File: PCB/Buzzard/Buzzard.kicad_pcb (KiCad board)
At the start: 2 copper layers, 152.1 x 94.5 mm, 87 parts, among them J1 PJ-320A, J2 LCD, J4 Haptic Buzz, J5 TrackPoint, J6 OLED, J8 Battery, SW1 SW_DPST_x2, SW2 Reset, U1 ProMicro, U10 Hole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

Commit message: diode placement
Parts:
- moved D11 247.8 mm to (170.7, 78.1), turned to -95 degrees
- moved D17 233.9 mm to (197.7, 79.4), turned to -110 degrees
- moved D18 216.2 mm to (190.9, 91.5), turned to -60 degrees
- moved D7 209.1 mm to (133.4, 81.8), turned to 90 degrees
- moved D3 202.6 mm to (116.4, 83.9), turned to -90 degrees
- moved D10 202.4 mm to (152.4, 76.9), turned to 90 degrees
- moved D2 200.9 mm to (116.4, 66.1), turned to -90 degrees
- moved D1 200.3 mm to (120.9, 60.6), turned to 180 degrees
- moved D6 198.7 mm to (145.6, 75.8), turned to 180 degrees
- moved D16 195.4 mm to (192.1, 76.7), turned to -100 degrees
- moved D15 192.5 mm to (182.3, 80.8), turned to -10 degrees
- moved D14 187.9 mm to (175.1, 73.9), turned to 80 degrees
- moved D13 186.3 mm to (177.3, 61.3), turned to 80 degrees
- moved D5 177.8 mm to (125.5, 48.8)
- moved D9 175.3 mm to (171.8, 64.1), turned to 85 degrees
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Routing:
- net Net-(D8-Pad2): track 30.7 -> 33.0 mm
- net TP_CLK: track 146.1 -> 144.0 mm
- net TP_DATA: track 140.6 -> 138.7 mm
- net COL2: track 142.5 -> 144.3 mm
- net ROW3: track 92.3 -> 93.6 mm
- net COL1: track 149.1 -> 150.2 mm

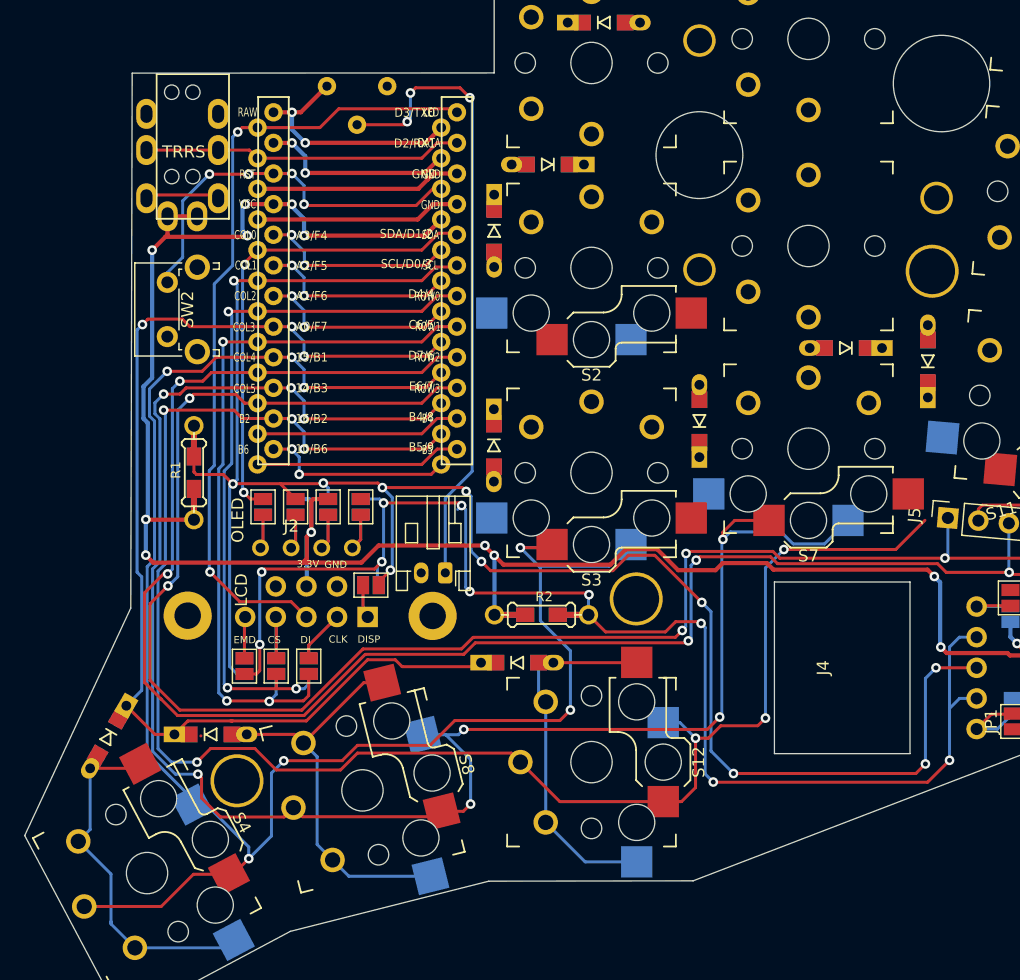
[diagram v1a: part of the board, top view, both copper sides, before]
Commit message: moved mcu and some rework
moved mcu more to the left
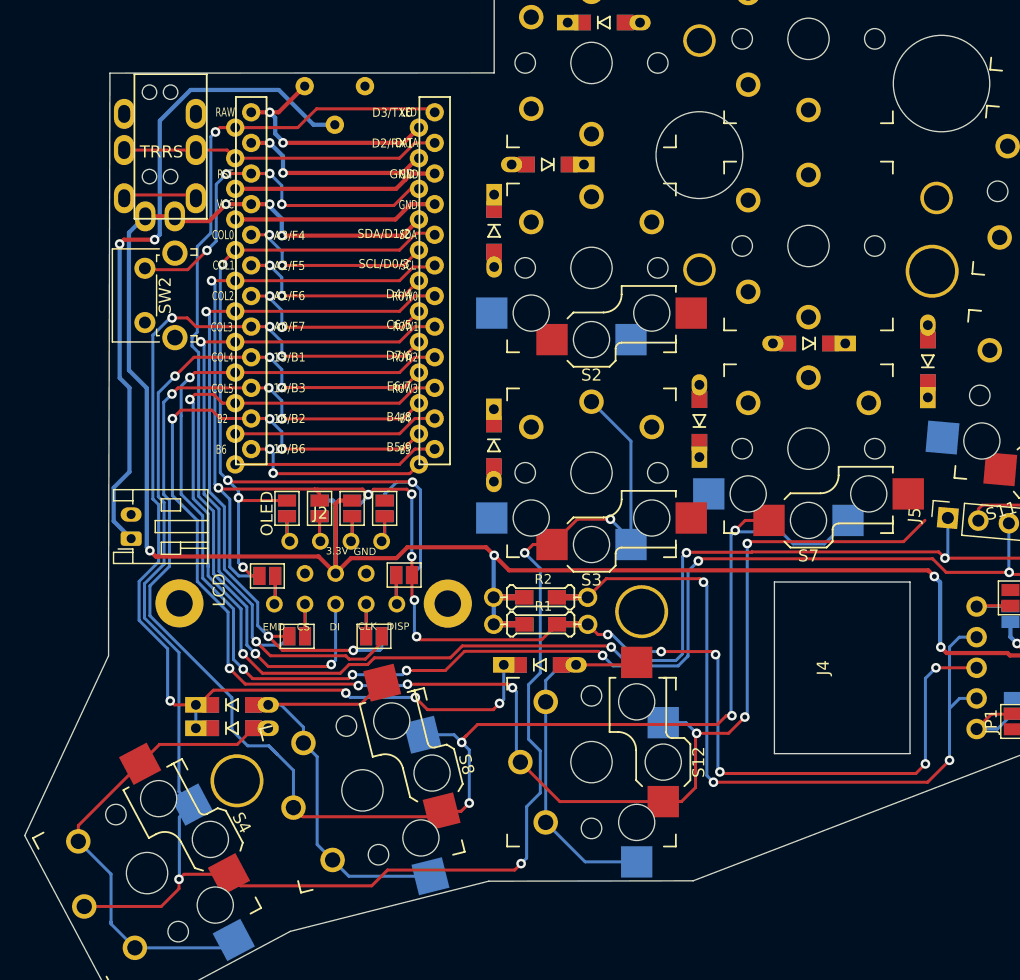
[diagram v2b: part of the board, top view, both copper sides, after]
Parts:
- moved R1 31.4 mm to (120.3, 98.7), turned to 180 degrees
- moved J8 26.2 mm to (86.3, 91.6), turned to 90 degrees
- moved D4 10.3 mm to (94.7, 107.3), turned to 0 degrees
- moved JP19 7.72 mm to (97.6, 94.7), turned to 0 degrees
- moved JP20 7.72 mm to (97.6, 94.7), turned to 0 degrees
- moved JP10 5.95 mm to (106.5, 99.7), turned to 180 degrees
- moved JP9 5.95 mm to (106.5, 99.7), turned to 180 degrees
- moved D6 3.07 mm to (142.6, 75.4)
- moved D8 3.03 mm to (94.7, 105.4)
- moved JP11 3.02 mm to (100.1, 99.7), turned to 0 degrees
- moved JP12 3.02 mm to (100.1, 99.7), turned to 0 degrees
- moved JP17 2.88 mm to (109.0, 94.6)
- moved JP18 2.88 mm to (109.0, 94.6)
- moved J2 2.65 mm to (103.3, 92.3)
- moved J6 2.49 mm to (103.3, 91.8)
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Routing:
- net SCL: track 160.0 -> 142.3 mm, vias 11 -> 13
- net SDA: track 153.9 -> 139.8 mm, vias 12 -> 8
- net COL0: track 149.9 -> 162.1 mm
- net TP_CLK: track 144.0 -> 132.7 mm, vias 5 -> 7
- net LCD_DI: track 66.1 -> 77.3 mm, vias 2 -> 3
- net TP_DATA: track 138.7 -> 128.0 mm
- net VCC: track 201.2 -> 190.8 mm, vias 13 -> 8
- net Net-(D4-Pad2): track 30.1 -> 39.1 mm
- net COL2: track 144.3 -> 135.5 mm, vias 7 -> 10
- net COL1: track 150.2 -> 143.1 mm, vias 8 -> 7
- net Net-(J2-Pad2): track 8.85 -> 5.40 mm
- net Net-(J8-Pad1): track 52.6 -> 55.8 mm, vias 3 -> 2
- net Net-(J2-Pad5): track 6.91 -> 4.73 mm
- net Net-(J6-Pad4): track 6.07 -> 4.37 mm
- net Net-(J6-Pad3): track 5.94 -> 4.23 mm
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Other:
- outline, holes or cut-outs redrawn

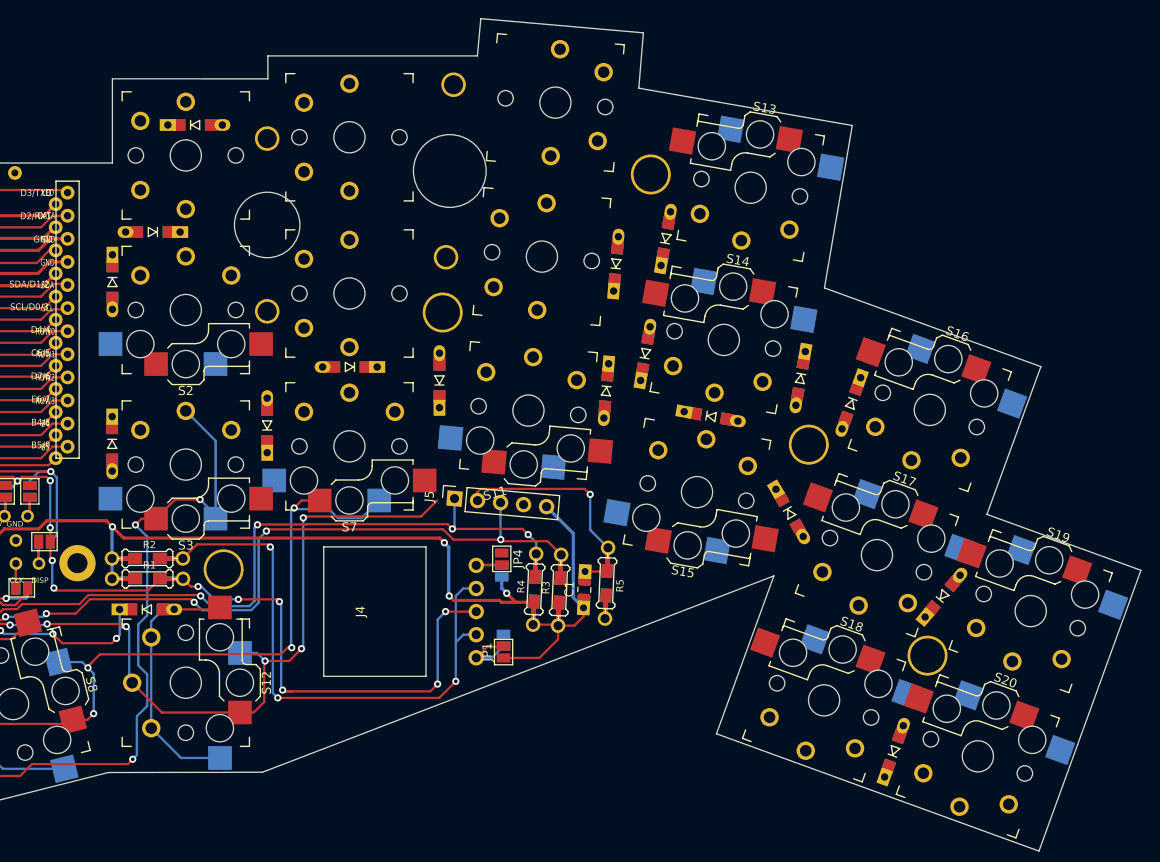
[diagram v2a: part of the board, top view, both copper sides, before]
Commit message: wiring of switches
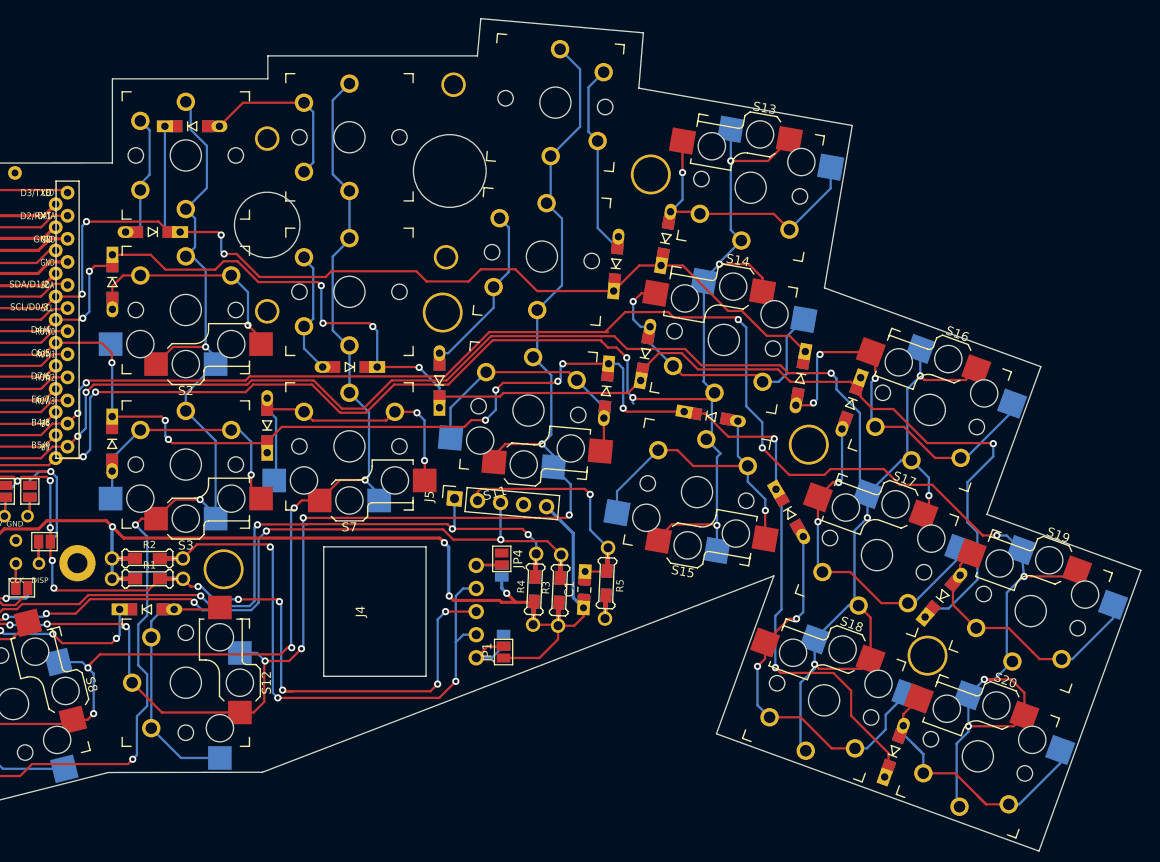
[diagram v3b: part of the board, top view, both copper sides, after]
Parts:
- moved D5 0.35 mm to (125.2, 48.9)
- moved S6 0.18 mm to (142.5, 67.2)
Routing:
- net COL4: track 17.1 -> 207.3 mm, vias 0 -> 7
- net COL5: track 17.1 -> 199.8 mm, vias 0 -> 8
- net COL3: track 16.1 -> 177.8 mm, vias 2 -> 9
- net ROW1: track 16.4 -> 166.7 mm, vias 2 -> 9
- net ROW2: track 16.5 -> 159.5 mm, vias 2 -> 12
- net ROW0: track 16.4 -> 128.3 mm, vias 2 -> 6
- net COL2: track 135.5 -> 214.2 mm, vias 10 -> 12
- net COL0: track 162.1 -> 208.2 mm, vias 7 -> 8
- net COL1: track 143.1 -> 189.2 mm, vias 7 -> 8
- net Net-(D18-Pad2): track 0.00 -> 42.9 mm, vias 0 -> 2
- net Net-(D16-Pad2): track 0.00 -> 41.9 mm, vias 0 -> 3
- net Net-(D17-Pad2): track 0.00 -> 36.9 mm, vias 0 -> 2
- net Net-(D7-Pad2): track 0.00 -> 33.7 mm, vias 0 -> 2
- net Net-(D15-Pad2): track 0.00 -> 33.5 mm, vias 0 -> 1
- net Net-(D14-Pad2): track 0.00 -> 32.7 mm, vias 0 -> 1
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
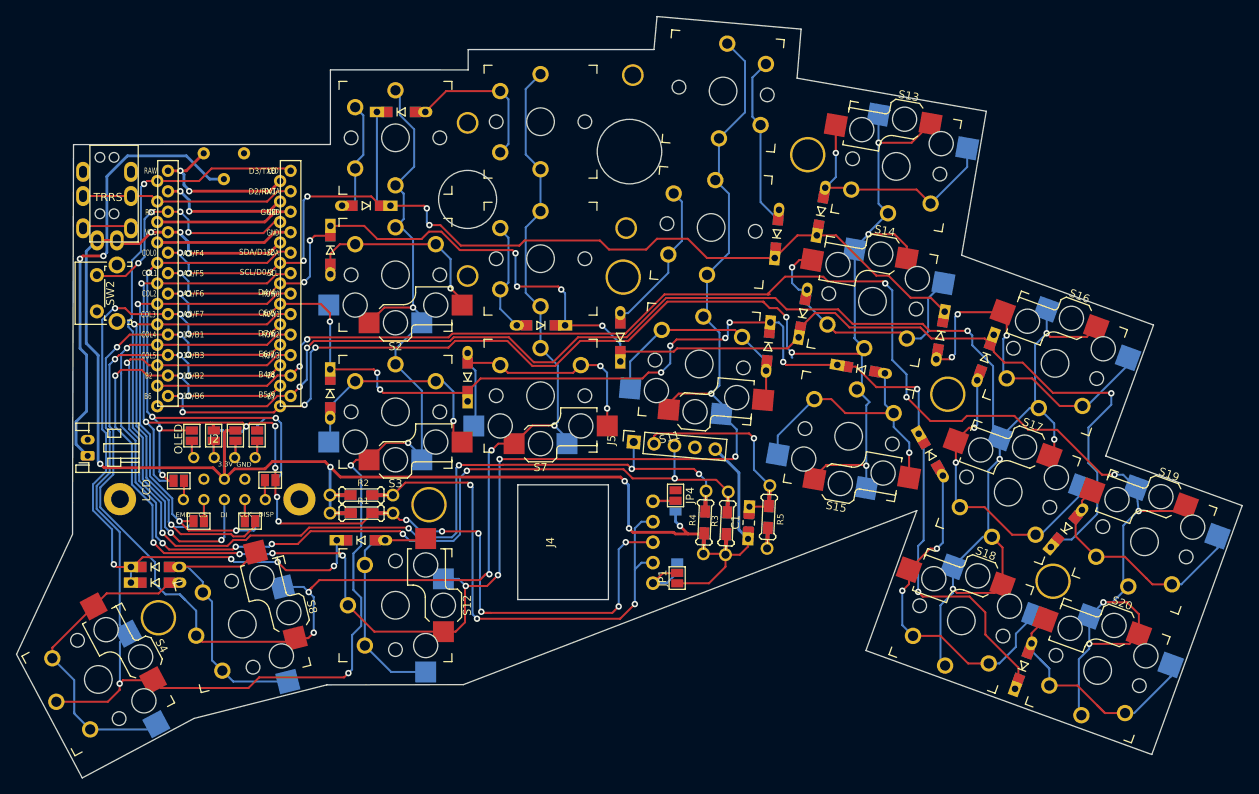
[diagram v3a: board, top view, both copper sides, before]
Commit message: rounded edge cuts
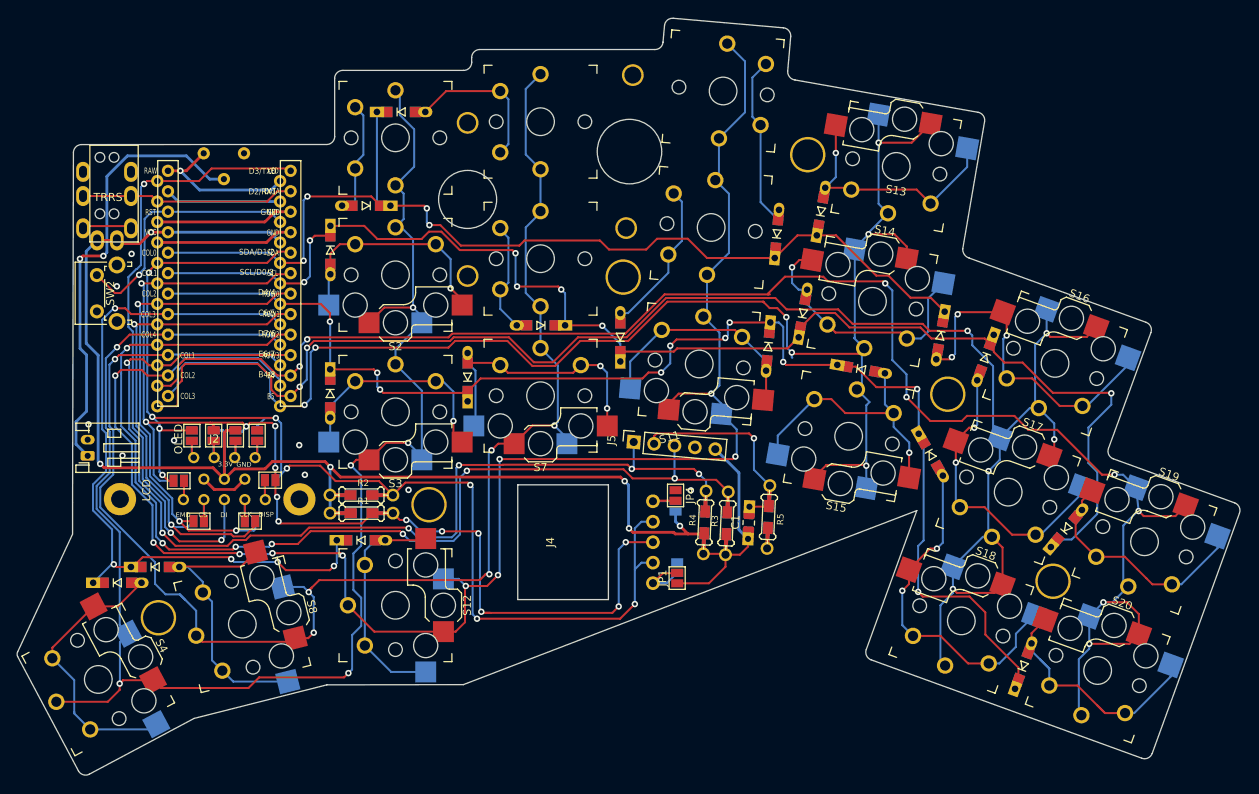
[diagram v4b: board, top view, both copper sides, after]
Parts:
- moved D4 4.69 mm to (90.0, 107.4)
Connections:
- J8 pad 2: BAT- -> GND
- U1 pad 23: BAT- -> GND
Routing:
- net GND: track 34.2 -> 54.9 mm, vias 0 -> 9
- net BAT-: track 16.3 -> 0.00 mm, vias 2 -> 0
- net SDA: track 139.8 -> 155.6 mm, vias 8 -> 9
- net COL4: track 207.3 -> 214.0 mm
- net COL3: track 177.8 -> 182.1 mm, vias 9 -> 7
- net Net-(D2-Pad2): track 23.8 -> 27.7 mm
- net Net-(D4-Pad2): track 39.1 -> 35.6 mm
- net COL5: track 199.8 -> 203.0 mm
- net VCC: track 190.8 -> 188.8 mm, vias 8 -> 6
- net ROW2: track 159.5 -> 157.4 mm, vias 12 -> 10
- net ROW1: track 166.7 -> 164.8 mm, vias 9 -> 7
- net ROW0: track 128.3 -> 126.4 mm, vias 6 -> 4
- net COL0: track 208.2 -> 206.3 mm, vias 8 -> 6
- net COL1: track 189.2 -> 187.3 mm, vias 8 -> 6
- net RESET: track 31.4 -> 32.7 mm, vias 4 -> 1
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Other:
- board size 152.1 x 94.5 mm -> 151.7 x 93.9 mm

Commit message: work on silk screen
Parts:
- renumbered J1 to Je, SW2 to Reset
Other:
- board text added: "CLK"
- board text added: "DAT"
- board text added: "GND"
- board text added: "Haptic Buzz"
- board text added: "OLED"
- board text added: "RST"
- board text added: "S10"
- board text added: "S5"
- board text added: "S6"
- board text added: "S9"
- board text added: "SCL"
- board text added: "SDA"
- board text added: "TrackPoint"
- board text added: "VCC"

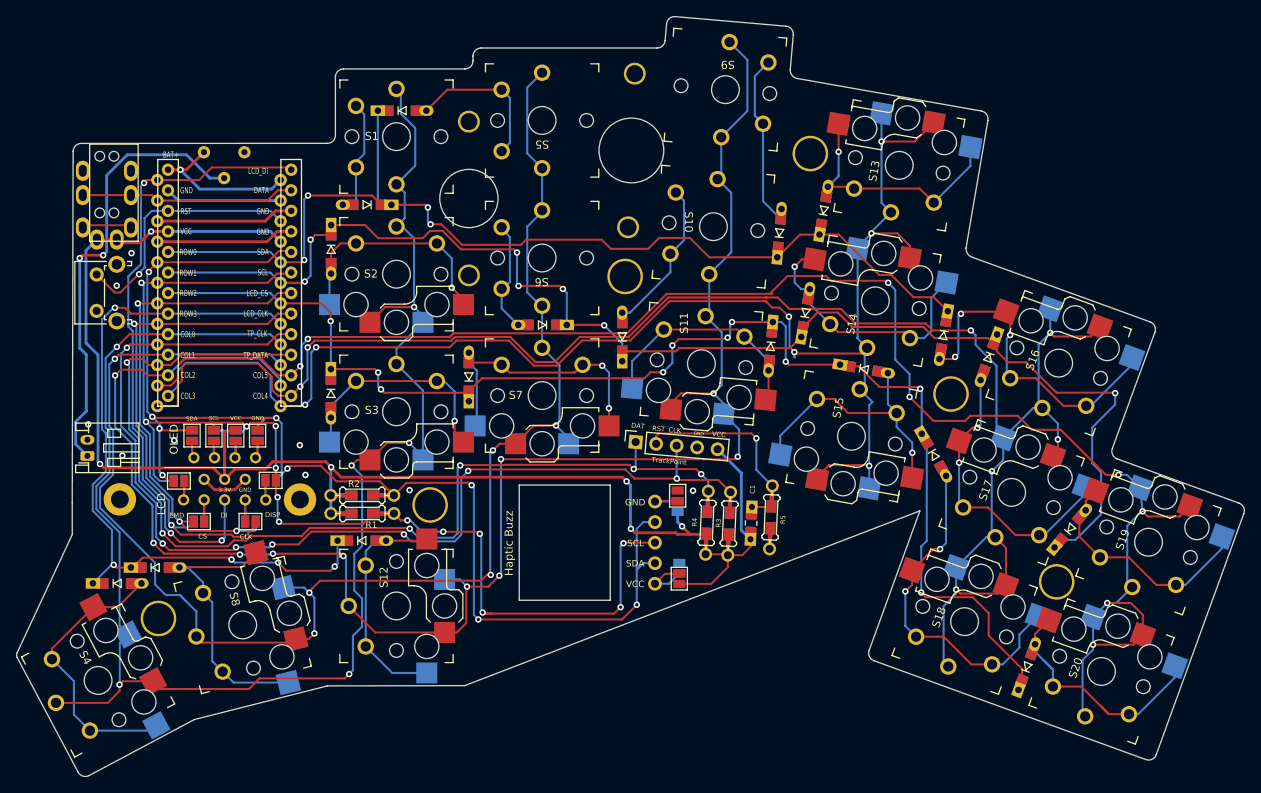
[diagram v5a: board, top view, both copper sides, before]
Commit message: fix errors and warnings
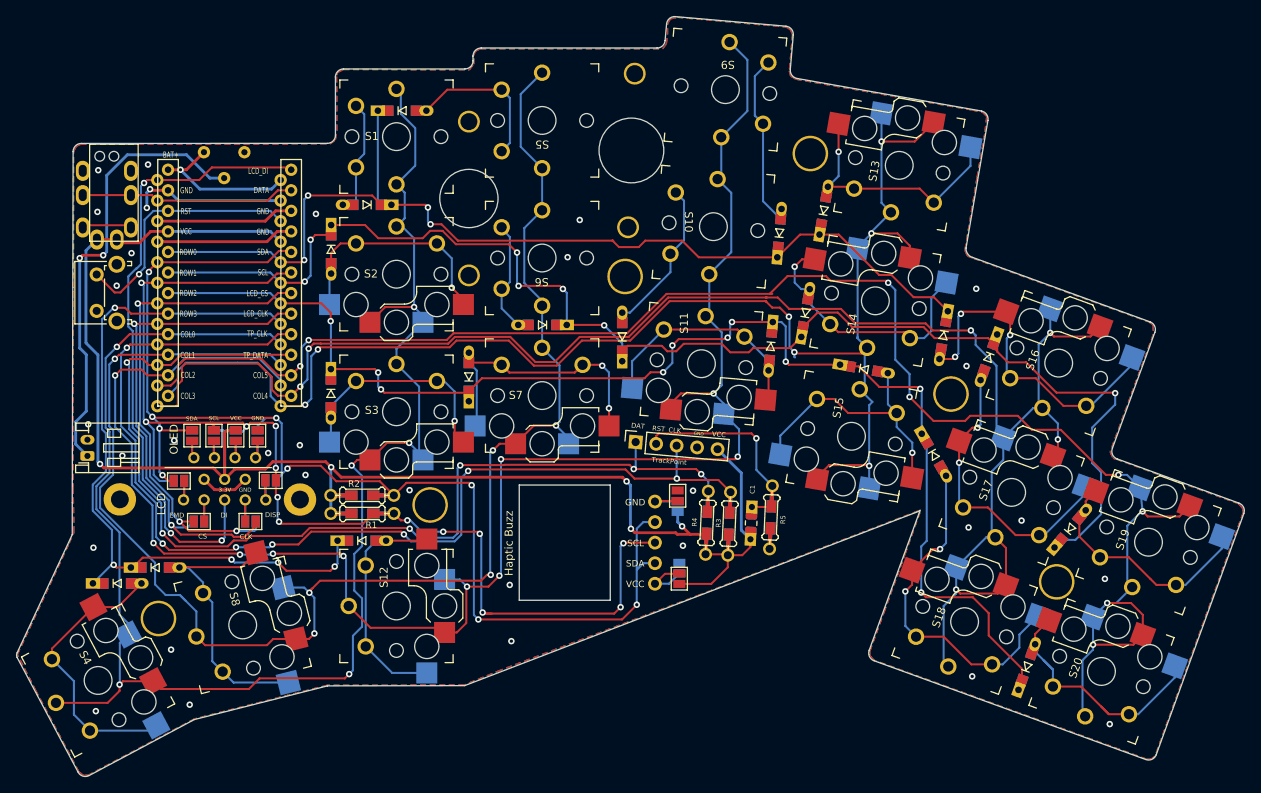
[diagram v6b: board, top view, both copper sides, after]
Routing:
- net GND: track 54.9 -> 59.6 mm, vias 9 -> 32
- net ROW1: track 164.8 -> 166.2 mm
- net COL1: track 187.3 -> 188.5 mm
- net ROW0: track 126.4 -> 125.6 mm
- net VCC: track 188.8 -> 188.9 mm, vias 6 -> 5
- net COL4: track 214.0 -> 213.8 mm, vias 7 -> 6
- added copper zone on B.Cu, net GND
- added copper zone on F.Cu, net GND
